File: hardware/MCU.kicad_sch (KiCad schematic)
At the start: 19 parts, among them U801 NUCLEO-L432KC, U802 TCAN1473A, U804 TLP241A

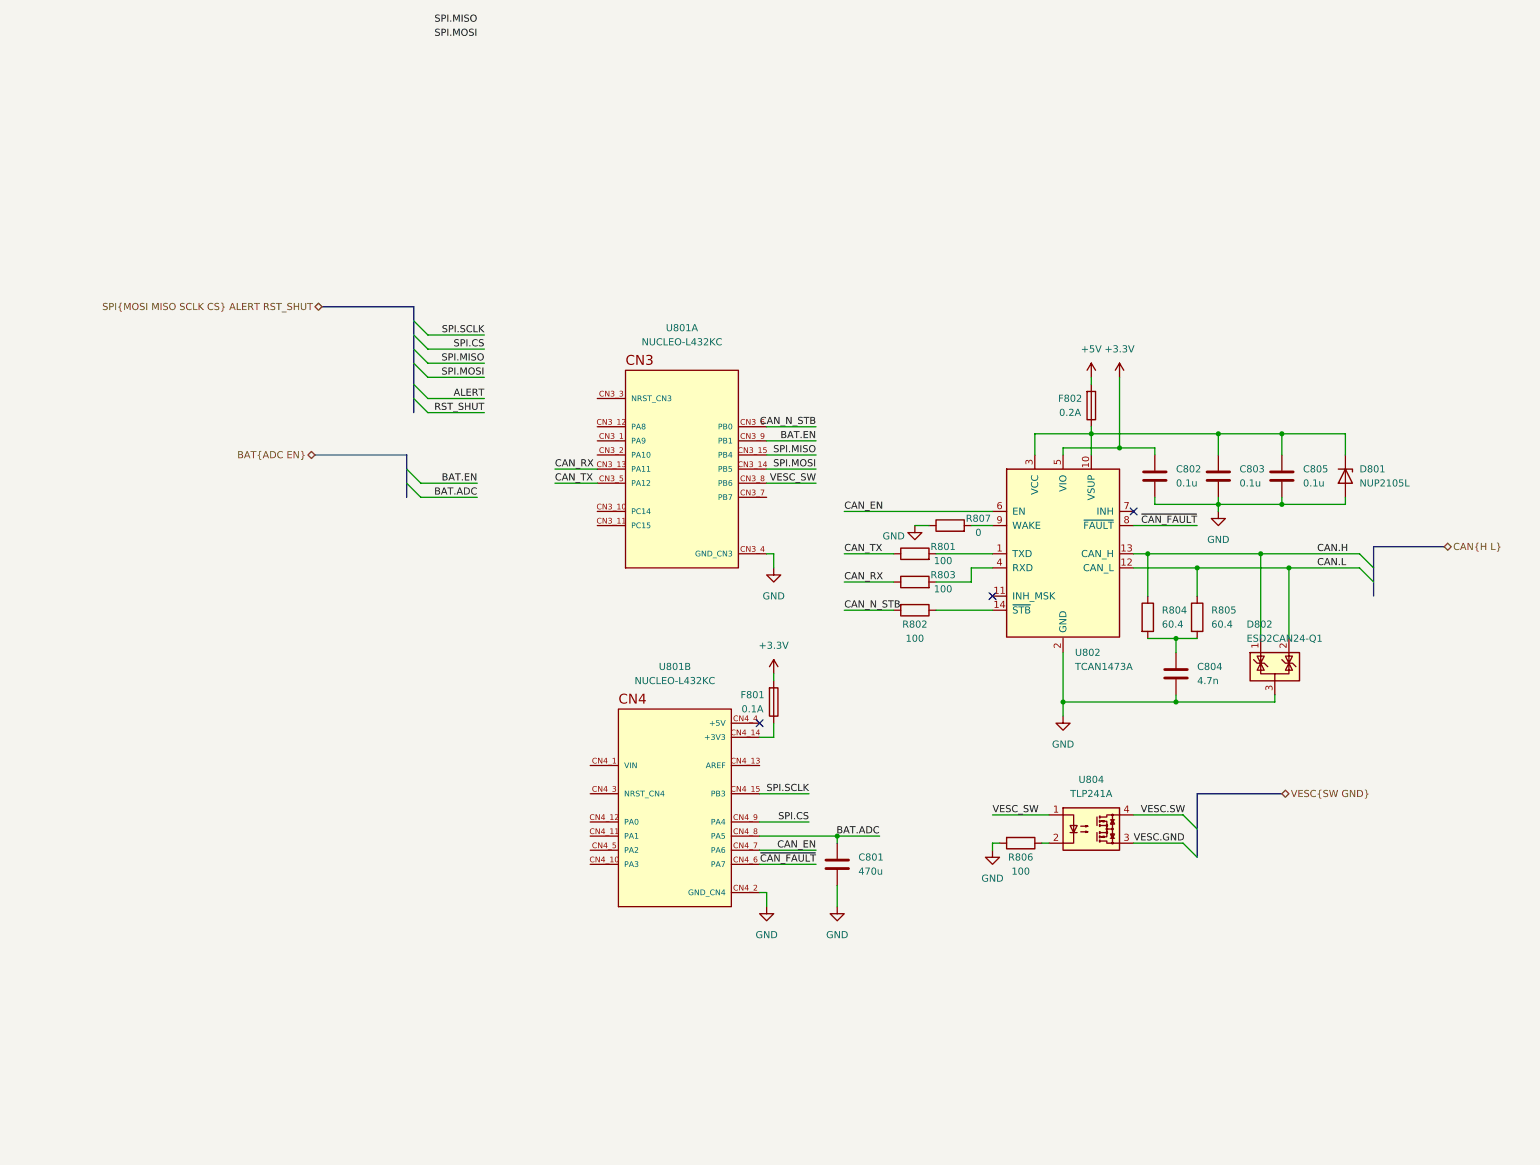
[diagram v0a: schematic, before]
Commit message: fix MCU pin mapping and resolve ERC conflicts
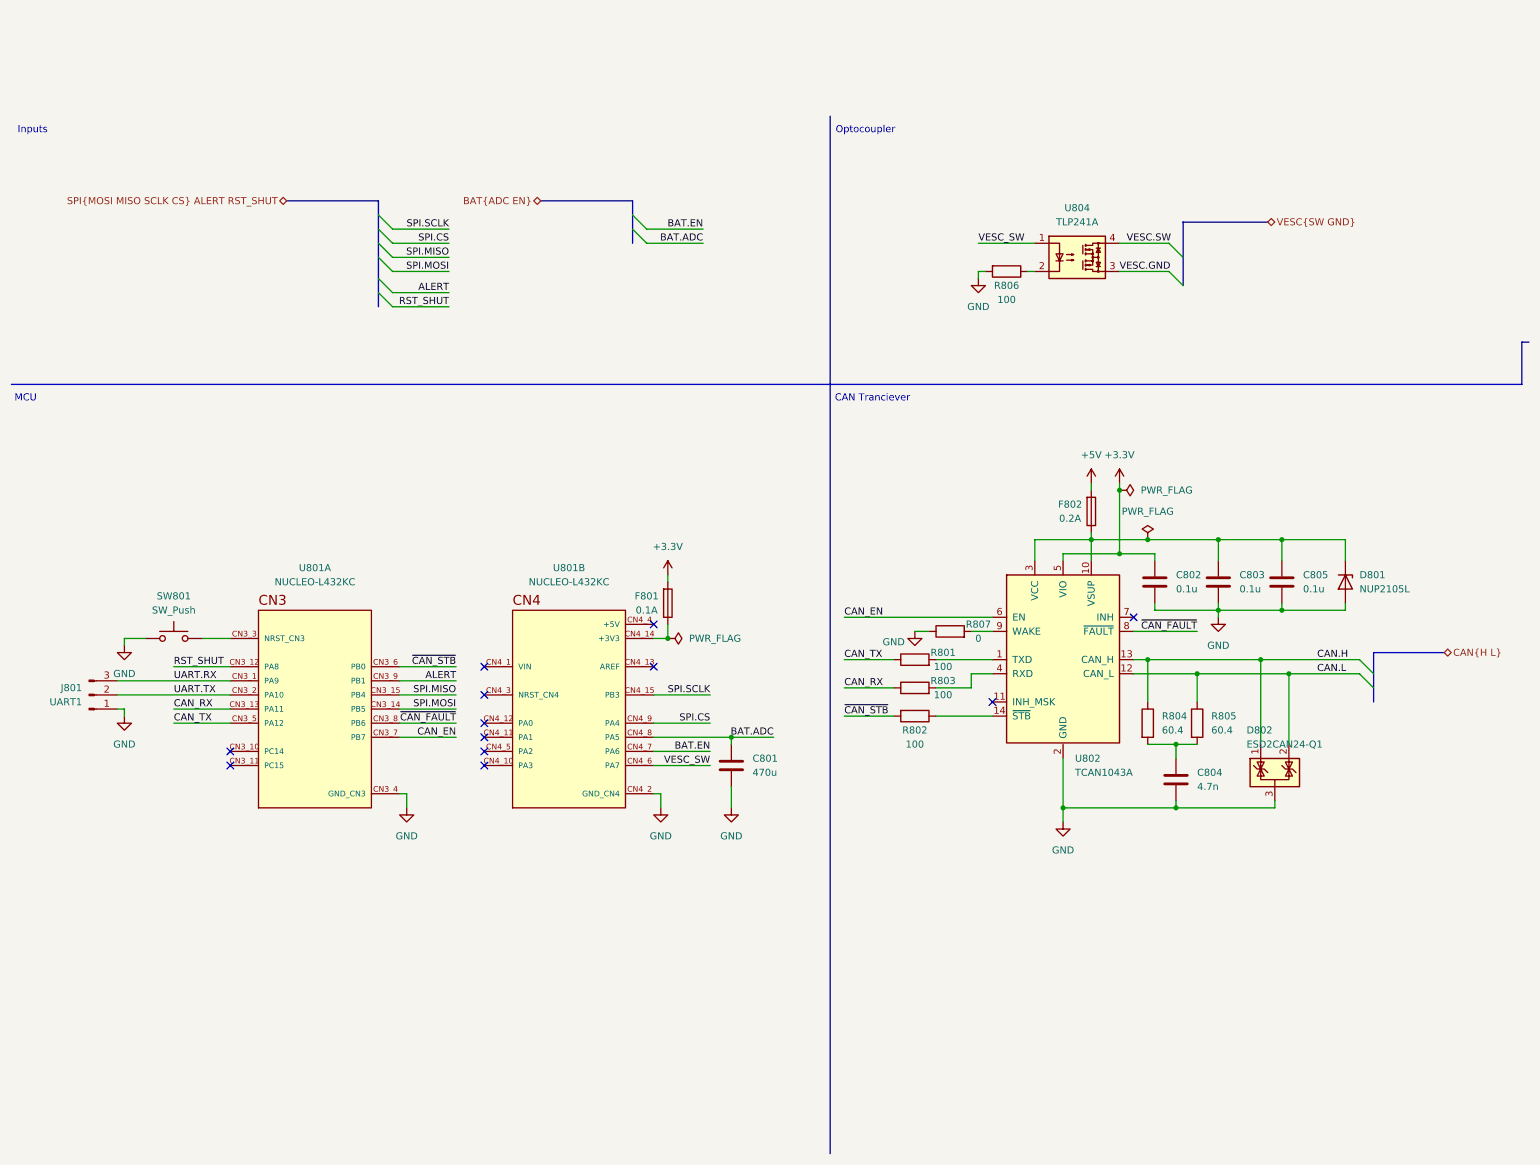
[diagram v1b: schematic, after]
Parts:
- added J801: UART1, Connector_JST:JST_EH_B3B-EH-A_1x03_P2.50mm_Vertical, symbol Connector:Conn_01x03_Pin
- added SW801: SW_Push, Button_Switch_SMD:SW_SPST_PTS810, symbol Switch:SW_Push
- U802: value TCAN1473A -> TCAN1043A; LCSC C38695 -> C5215847; LCSC_Alt1 C2671057 -> C1848115; MPN TJA1051T/3/1J -> TCAN1043ADRQ1; MPN_Alt1 TCAN1042HDRQ1 -> TCAN1043GDRQ1; MPN_Alt2 (none) -> TCAN843-Q1
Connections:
- net ALERT: now also U801.CN3_9 (PB1)
- net BAT.EN: now also U801.CN4_7 (PA6); no longer U801.CN3_9 (PB1)
- net CAN_EN: now also U801.CN3_7 (PB7); no longer U801.CN4_7 (PA6)
- net GND: now also J801.1 (Pin_1), SW801.1
- net RST_SHUT: now also U801.CN3_12 (PA8)
- net VESC_SW: now also U801.CN4_6 (PA7); no longer U801.CN3_8 (PB6)
- net ~{CAN_FAULT}: now also U801.CN3_8 (PB6); no longer U801.CN4_6 (PA7)
- net UART.RX: now reaches U801.CN3_1 (PA9)
- net UART.RX: now also J801.3 (Pin_3)
- net UART.TX: now reaches U801.CN3_2 (PA10)
- net UART.TX: now also J801.2 (Pin_2)
- net at U801.CN3_3 (NRST_CN3): now also SW801.2
- net CAN_N_STB renamed ~{CAN_STB}
- no-connect marks 3 -> 12
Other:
- note added: "CAN Tranciever"
- note added: "Inputs"
- note added: "MCU"
- note added: "Optocoupler"
- moved on the sheet: C801, C802, C803, C804, C805, D801, D802, F801, F802, R801, R802, R803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

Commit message: use bus alias
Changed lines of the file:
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@@
+		)
+	)
+	(label "ALERT"
+		(at 92.71 113.03 180)
+		(effects
+			(font
+				(size 1.27 1.27)
+			)
+			(justify right bottom)
 		)
 	)
@@
 		)
 	)
-	(label "ALERT"
-		(at 92.71 113.03 180)
-		(effects
-			(font
-				(size 1.27 1.27)
-			)
-			(justify right bottom)
-		)
-	)
 	(label "RST_SHUT"
 		(at 41.91 110.49 0)
@@
 		)
 	)
-	(hierarchical_label "SPI{MOSI MISO SCLK CS} ALERT RST_SHUT"
+	(hierarchical_label "{AFE_CTRL}"
 		(shape bidirectional)
 		(at 62.23 26.67 180)

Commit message: fix ERC warnings and footprint issues
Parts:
- U801: footprint NUCLEO-L432KC:MODULE_NUCLEO-L432KC -> wafel-eval-board:MODULE_NUCLEO-L432KC

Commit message: update schematics
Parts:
- U801: footprint wafel-eval-board:MODULE_NUCLEO-L432KC -> NUCLEO-L432KC:MODULE_NUCLEO-L432KC

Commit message: fix remaining missing footprints
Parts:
- U801: footprint NUCLEO-L432KC:MODULE_NUCLEO-L432KC -> wafel-eval-board:MODULE_NUCLEO-L432KC
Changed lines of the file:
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@@
 			)
 		)
-		(property "Footprint" "NUCLEO-L432KC:MODULE_NUCLEO-L432KC"
+		(property "Footprint" "wafel-eval-board:MODULE_NUCLEO-L432KC"
 			(at 113.03 118.11 0)
 			(hide yes)
@@
 			)
 		)
-		(property "Footprint" "NUCLEO-L432KC:MODULE_NUCLEO-L432KC"
+		(property "Footprint" "wafel-eval-board:MODULE_NUCLEO-L432KC"
 			(at 67.31 118.11 0)
 			(hide yes)

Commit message: placed c mosfet
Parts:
- C801, C802, C805: footprint Capacitor_SMD:C_0805_2012Metric -> Capacitor_SMD:C_0603_1608Metric
- C803: renamed from C804; footprint Capacitor_SMD:C_0805_2012Metric -> Capacitor_SMD:C_0603_1608Metric
- C804: renamed from C803; footprint Capacitor_SMD:C_0805_2012Metric -> Capacitor_SMD:C_0603_1608Metric
- R801: footprint Resistor_SMD:R_0805_2012Metric -> Resistor_SMD:R_0603_1608Metric
- R802: renamed from R803; footprint Resistor_SMD:R_0805_2012Metric -> Resistor_SMD:R_0603_1608Metric
- R803: renamed from R802; footprint Resistor_SMD:R_0805_2012Metric -> Resistor_SMD:R_0603_1608Metric
- R804: renamed from R807; footprint Resistor_SMD:R_0805_2012Metric -> Resistor_SMD:R_0603_1608Metric
- R805: renamed from R806; footprint Resistor_SMD:R_0805_2012Metric -> Resistor_SMD:R_0603_1608Metric
- R806: renamed from R804; footprint Resistor_SMD:R_0805_2012Metric -> Resistor_SMD:R_0603_1608Metric
- R807: renamed from R805; footprint Resistor_SMD:R_0805_2012Metric -> Resistor_SMD:R_0603_1608Metric
- renumbered D802 to D801, D801 to D802, U804 to U803

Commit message: reduced BOM
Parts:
- C801: value 470u -> 470n
- C802, C804, C805: value 0.1u -> 100n
- U802: footprint (none) -> Package_SO:SOIC-14_3.9x8.7mm_P1.27mm
